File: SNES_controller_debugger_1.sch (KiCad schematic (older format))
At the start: 21 parts, among them J1 ICSP, J2 CONTROLLER_OUT, J3 MICRO_USB, SW1 Reset_switch, U1 ATmega32U4, Y1 16MHz

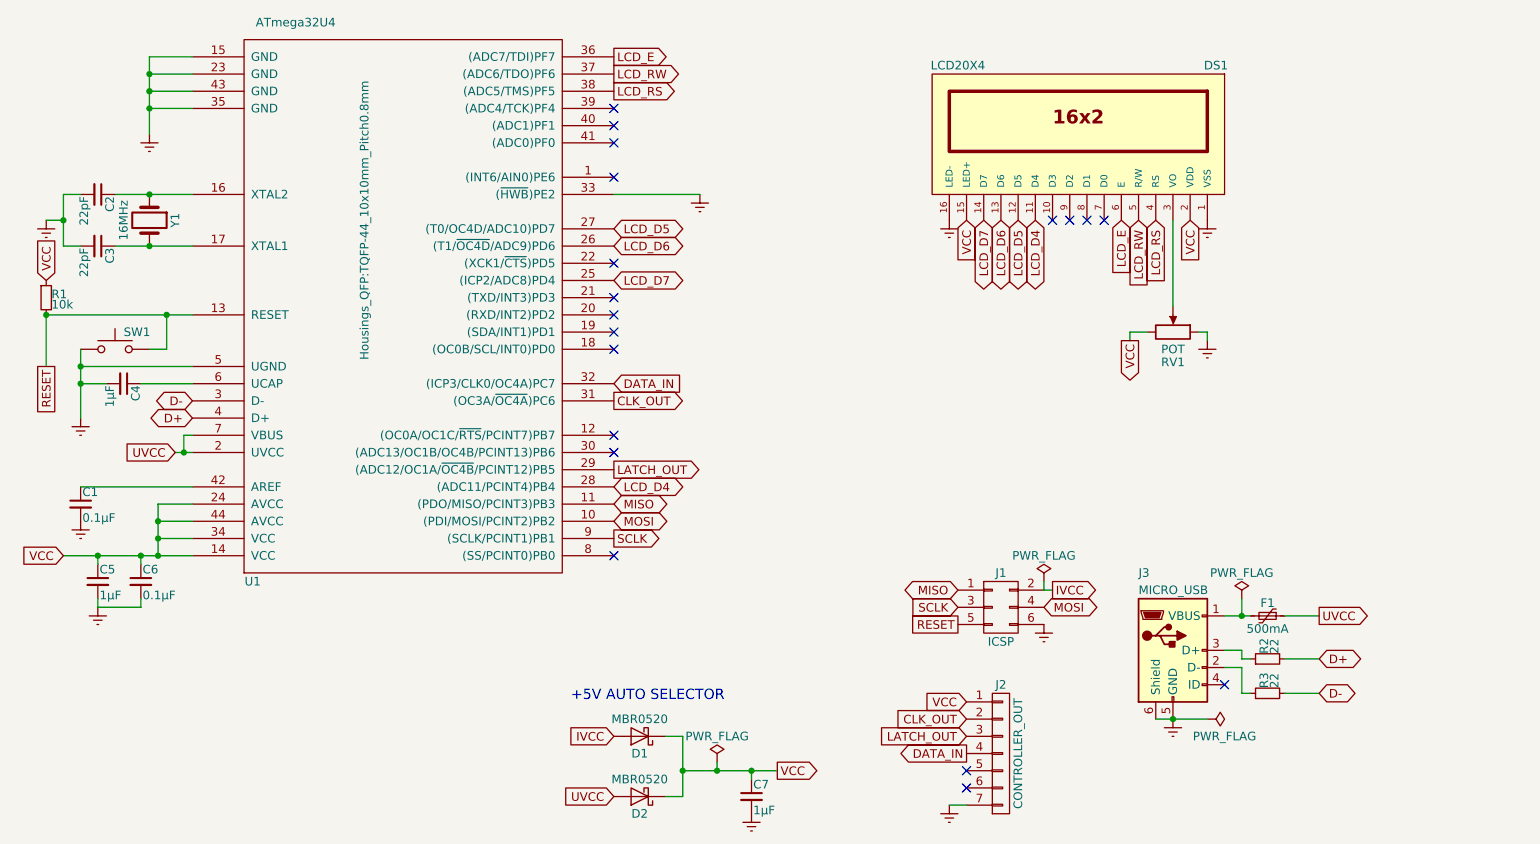
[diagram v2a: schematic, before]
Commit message: pcb: Add hardware capability to dim the LCD backlight and to switch power to the LCD
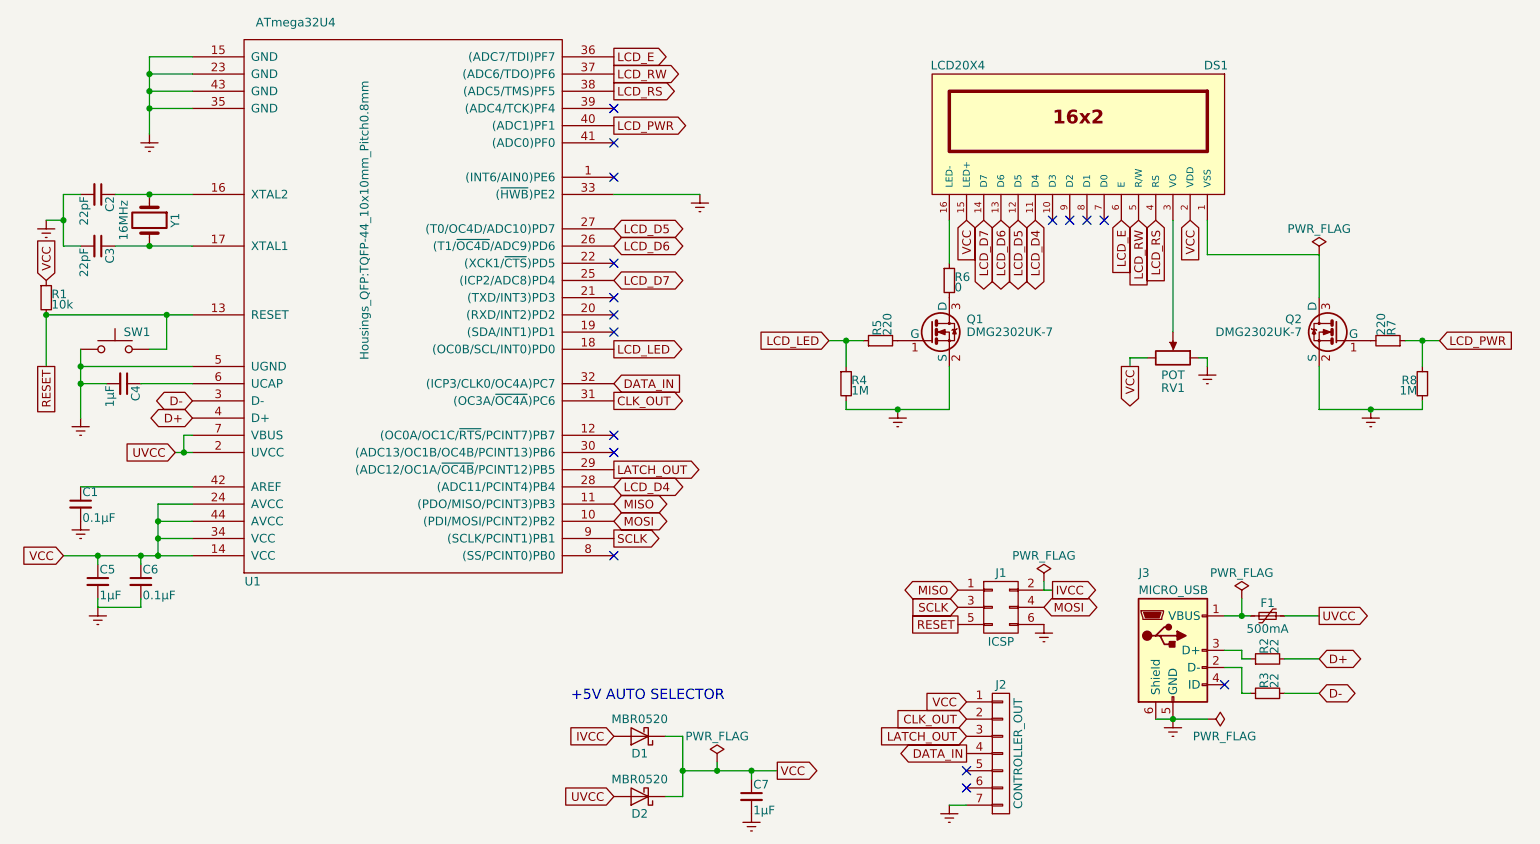
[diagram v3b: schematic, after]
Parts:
- added Q1, Q2: DMG2302UK-7, TO_SOT_Packages_SMD:SOT-23, symbol BSS138
- added R4, R8: 1M, Resistors_SMD:R_0603_HandSoldering, symbol R_Small
- added R5, R7: 220, Resistors_SMD:R_0603_HandSoldering, symbol R_Small
- added R6: 0, Resistors_SMD:R_0603_HandSoldering, symbol R_Small
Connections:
- net Earth: now also Q1.2 (S), Q2.2 (S), R4.2, R8.2; no longer DS1.1 (VSS), DS1.16 (LED-)
- net LCD_LED: now reaches U1.18 ((OC0B/SCL/INT0)PD0)
- net LCD_LED: now also R4.1, R5.1
- net LCD_PWR: now reaches U1.40 ((ADC1)PF1)
- net LCD_PWR: now also R7.1, R8.1
- new net: DS1.1 (VSS), Q2.3 (D)
- new net: DS1.16 (LED-), R6.1
- new net: Q1.3 (D), R6.2
- new net: Q1.1 (G), R5.2
- new net: Q2.1 (G), R7.2
- no-connect marks 19 -> 17
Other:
- moved on the sheet: RV1
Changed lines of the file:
@@
 L POT RV1
 U 1 1 591B92F6
-P 7200 3200
-F 0 "RV1" V 7025 3200 50  0000 C CNN
-F 1 "POT" V 7100 3200 50  0000 C CNN
-F 2 "Megaris_fixed_footprints:Potentiometer_Trimmer_Vishay_TS53YL" H 7200 3200 50  0001 C CNN
-F 3 "" H 7200 3200 50  0001 C CNN
-F 4 "TS53YL-10KCT-ND" V 7200 3200 60  0001 C CNN "Digi-Key part number"
-F 5 "TS53YL103MR10" V 7200 3200 60  0001 C CNN "MPN"
-	1    7200 3200
+P 7200 3350
+F 0 "RV1" V 7025 3350 50  0000 C CNN
+F 1 "POT" V 7100 3350 50  0000 C CNN
+F 2 "Megaris_fixed_footprints:Potentiometer_Trimmer_Vishay_TS53YL" H 7200 3350 50  0001 C CNN
+F 3 "" H 7200 3350 50  0001 C CNN
+F 4 "TS53YL-10KCT-ND" V 7200 3350 60  0001 C CNN "Digi-Key part number"
+F 5 "TS53YL103MR10" V 7200 3350 60  0001 C CNN "MPN"
+	1    7200 3350
 	0    1    -1   0
 $EndComp
@@
 $EndComp
 NoConn ~ 3950 1900
-NoConn ~ 3950 2000
 NoConn ~ 3950 2100
 NoConn ~ 3950 2300
-NoConn ~ 3950 2800
-NoConn ~ 3950 3300
 NoConn ~ 3950 3800
 NoConn ~ 3950 3900
@@
 $Comp
 L Earth #PWR01
-U 1 1 591D4C41
-P 7400 2550
-F 0 "#PWR01" H 7400 2300 50  0001 C CNN
-F 1 "Earth" H 7400 2400 50  0001 C CNN
-F 2 "" H 7400 2550 50  0001 C CNN
-F 3 "" H 7400 2550 50  0001 C CNN
-	1    7400 2550
-	1    0    0    -1
-$EndComp
-$Comp
-L Earth #PWR02
-U 1 1 591D4E59
-P 5900 2550
-F 0 "#PWR02" H 5900 2300 50  0001 C CNN
-F 1 "Earth" H 5900 2400 50  0001 C CNN
-F 2 "" H 5900 2550 50  0001 C CNN
-F 3 "" H 5900 2550 50  0001 C CNN
-	1    5900 2550
-	1    0    0    -1
-$EndComp
-$Comp
-L Earth #PWR03
 U 1 1 591D50E7
-P 7400 3250
-F 0 "#PWR03" H 7400 3000 50  0001 C CNN
-F 1 "Earth" H 7400 3100 50  0001 C CNN
-F 2 "" H 7400 3250 50  0001 C CNN
-F 3 "" H 7400 3250 50  0001 C CNN
-	1    7400 3250
+P 7400 3400
+F 0 "#PWR01" H 7400 3150 50  0001 C CNN
+F 1 "Earth" H 7400 3250 50  0001 C CNN
+F 2 "" H 7400 3400 50  0001 C CNN
+F 3 "" H 7400 3400 50  0001 C CNN
+	1    7400 3400
 	1    0    0    -1
 $EndComp
@@
 $EndComp
 $Comp
-L Earth #PWR04
+L Earth #PWR02
 U 1 1 591D5F38
 P 6450 4900
-F 0 "#PWR04" H 6450 4650 50  0001 C CNN
+F 0 "#PWR02" H 6450 4650 50  0001 C CNN
 F 1 "Earth" H 6450 4750 50  0001 C CNN
 F 2 "" H 6450 4900 50  0001 C CNN
@@
 $EndComp
 $Comp
-L Earth #PWR05
+L Earth #PWR03
 U 1 1 591D6035
 P 5900 5950
-F 0 "#PWR05" H 5900 5700 50  0001 C CNN
+F 0 "#PWR03" H 5900 5700 50  0001 C CNN
 F 1 "Earth" H 5900 5800 50  0001 C CNN
 F 2 "" H 5900 5950 50  0001 C CNN
@@
 $EndComp
 $Comp
-L Earth #PWR06
+L Earth #PWR04
 U 1 1 591D683F
 P 7200 5450
-F 0 "#PWR06" H 7200 5200 50  0001 C CNN
+F 0 "#PWR04" H 7200 5200 50  0001 C CNN
 F 1 "Earth" H 7200 5300 50  0001 C CNN
 F 2 "" H 7200 5450 50  0001 C CNN
@@
 NoConn ~ 3950 3100
 $Comp
-L PWR_FLAG #FLG07
+L PWR_FLAG #FLG05
 U 1 1 591D9550
 P 7400 5450
-F 0 "#FLG07" H 7400 5525 50  0001 C CNN
+F 0 "#FLG05" H 7400 5525 50  0001 C CNN
 F 1 "PWR_FLAG" V 7500 5550 50  0000 C CNN
 F 2 "" H 7400 5450 50  0001 C CNN
@@
 $EndComp
 $Comp
-L Earth #PWR08
+L Earth #PWR06
 U 1 1 591D9AF5
 P 650 2550
-F 0 "#PWR08" H 650 2300 50  0001 C CNN
+F 0 "#PWR06" H 650 2300 50  0001 C CNN
 F 1 "Earth" H 650 2400 50  0001 C CNN
 F 2 "" H 650 2550 50  0001 C CNN
@@
 $EndComp
 $Comp
-L Earth #PWR09
+L Earth #PWR07
 U 1 1 591D9C68
 P 850 3700
-F 0 "#PWR09" H 850 3450 50  0001 C CNN
+F 0 "#PWR07" H 850 3450 50  0001 C CNN
 F 1 "Earth" H 850 3550 50  0001 C CNN
 F 2 "" H 850 3700 50  0001 C CNN
@@
 $EndComp
 $Comp
-L Earth #PWR010
+L Earth #PWR08
 U 1 1 591D9CB5
 P 1250 2050
-F 0 "#PWR010" H 1250 1800 50  0001 C CNN
+F 0 "#PWR08" H 1250 1800 50  0001 C CNN
 F 1 "Earth" H 1250 1900 50  0001 C CNN
 F 2 "" H 1250 2050 50  0001 C CNN
@@
 $EndComp
 $Comp
-L Earth #PWR011
+L Earth #PWR09
 U 1 1 591D9D04
 P 850 4300
-F 0 "#PWR011" H 850 4050 50  0001 C CNN
+F 0 "#PWR09" H 850 4050 50  0001 C CNN
 F 1 "Earth" H 850 4150 50  0001 C CNN
 F 2 "" H 850 4300 50  0001 C CNN
@@
 $EndComp
 $Comp
-L PWR_FLAG #FLG012
+L PWR_FLAG #FLG010
 U 1 1 591DA503
 P 7600 4750
-F 0 "#FLG012" H 7600 4825 50  0001 C CNN
+F 0 "#FLG010" H 7600 4825 50  0001 C CNN
 F 1 "PWR_FLAG" H 7600 4900 50  0000 C CNN
 F 2 "" H 7600 4750 50  0001 C CNN
@@
 Text GLabel 3950 3500 2    50   Input ~ 0
 DATA_IN
-NoConn ~ 3950 3200
 $Comp
 L Polyfuse_Small F1
@@
 Text GLabel 7300 2550 3    50   Input ~ 0
 VCC
-Text GLabel 6000 2550 3    50   Input ~ 0
-VCC
-Text GLabel 6950 3250 3    50   Output ~ 0
+Text GLabel 6950 3400 3    50   Output ~ 0
 VCC
 Text GLabel 750  4500 0    50   Input ~ 0
@@
 IVCC
 $Comp
-L PWR_FLAG #FLG013
+L PWR_FLAG #FLG011
 U 1 1 591FC2B2
 P 6450 4650
-F 0 "#FLG013" H 6450 4725 50  0001 C CNN
+F 0 "#FLG011" H 6450 4725 50  0001 C CNN
 F 1 "PWR_FLAG" H 6450 4800 50  0000 C CNN
 F 2 "" H 6450 4650 50  0001 C CNN
@@
 VCC
 $Comp
-L PWR_FLAG #FLG014
+L PWR_FLAG #FLG012
 U 1 1 591FEDEE
 P 4550 5700
-F 0 "#FLG014" H 4550 5775 50  0001 C CNN
+F 0 "#FLG012" H 4550 5775 50  0001 C CNN
 F 1 "PWR_FLAG" H 4550 5850 50  0000 C CNN
 F 2 "" H 4550 5700 50  0001 C CNN
@@
 $EndComp
 $Comp
-L Earth #PWR015
+L Earth #PWR013
 U 1 1 59301178
 P 4450 2400
-F 0 "#PWR015" H 4450 2150 50  0001 C CNN
+F 0 "#PWR013" H 4450 2150 50  0001 C CNN
 F 1 "Earth" H 4450 2250 50  0001 C CNN
 F 2 "" H 4450 2400 50  0001 C CNN
@@
 $EndComp
 $Comp
-L Earth #PWR016
+L Earth #PWR014
 U 1 1 593021E9
 P 4750 6000
-F 0 "#PWR016" H 4750 5750 50  0001 C CNN
+F 0 "#PWR014" H 4750 5750 50  0001 C CNN
 F 1 "Earth" H 4750 5850 50  0001 C CNN
 F 2 "" H 4750 6000 50  0001 C CNN
@@
 $EndComp
 $Comp
-L Earth #PWR017
+L Earth #PWR015
 U 1 1 593033E6
 P 950 4800
-F 0 "#PWR017" H 950 4550 50  0001 C CNN
+F 0 "#PWR015" H 950 4550 50  0001 C CNN
 F 1 "Earth" H 950 4650 50  0001 C CNN
 F 2 "" H 950 4800 50  0001 C CNN
@@
 	1    0    0    -1
 $EndComp
+Text GLabel 3950 3300 2    50   Output ~ 0
+LCD_LED
 Wire Wire Line
 	6450 4650 6450 4700
@@
 	4350 5900 4250 5900
 Wire Wire Line
-	6950 3200 6950 3250
+	6950 3350 6950 3400
 Connection ~ 7200 5450
 Wire Wire Line
@@
 Connection ~ 1250 1700
 Wire Wire Line
-	7200 3050 7200 2550
-Wire Wire Line
-	7350 3200 7400 3200
-Wire Wire Line
-	7400 3200 7400 3250
-Wire Wire Line
-	7050 3200 6950 3200
+	7350 3350 7400 3350
+Wire Wire Line
+	7400 3350 7400 3400
+Wire Wire Line
+	7050 3350 6950 3350
 Wire Wire Line
 	1250 1600 1250 2050
@@
 	1500 4200 1300 4200
 Wire Wire Line
-	1300 4500 1300 4200
+	1300 4200 1300 4500
 Connection ~ 1300 4500
 Wire Wire Line
@@
 Wire Wire Line
 	7600 5100 7650 5100
+$Comp
+L R_Small R6
+U 1 1 598B7C95
+P 5900 2900
+F 0 "R6" H 5930 2920 50  0000 L CNN
+F 1 "0" H 5930 2860 50  0000 L CNN
+F 2 "Resistors_SMD:R_0603_HandSoldering" H 5900 2900 50  0001 C CNN
+F 3 "" H 5900 2900 50  0001 C CNN
+	1    5900 2900
+	1    0    0    -1
+$EndComp
+$Comp
+L Earth #PWR016
+U 1 1 598B7F8F
+P 5600 3650
+F 0 "#PWR016" H 5600 3400 50  0001 C CNN
+F 1 "Earth" H 5600 3500 50  0001 C CNN
+F 2 "" H 5600 3650 50  0001 C CNN
+F 3 "" H 5600 3650 50  0001 C CNN
+	1    5600 3650
+	1    0    0    -1
+$EndComp
+Text GLabel 6000 2550 3    50   Input ~ 0
+VCC
+Text GLabel 5200 3250 0    50   Input ~ 0
+LCD_LED
+$Comp
+L R_Small R5
+U 1 1 598B82E3
+P 5500 3250
+F 0 "R5" H 5530 3270 50  0000 L CNN
+F 1 "220" H 5530 3210 50  0000 L CNN
+F 2 "Resistors_SMD:R_0603_HandSoldering" H 5500 3250 50  0001 C CNN
+F 3 "" H 5500 3250 50  0001 C CNN
+	1    5500 3250
+	0    -1   -1   0
+$EndComp
+$Comp
+L BSS138 Q1
+U 1 1 598C915B
+P 5800 3200
+F 0 "Q1" H 6000 3275 50  0000 L CNN
+F 1 "DMG2302UK-7" H 6000 3200 50  0000 L CNN
+F 2 "TO_SOT_Packages_SMD:SOT-23" H 6000 3125 50  0001 L CIN
+F 3 "" H 5800 3200 50  0001 L CNN
+	1    5800 3200
+	1    0    0    -1
+$EndComp
+$Comp
+L R_Small R4
+U 1 1 598C9414
+P 5300 3500
+F 0 "R4" H 5330 3520 50  0000 L CNN
+F 1 "1M" H 5330 3460 50  0000 L CNN
+F 2 "Resistors_SMD:R_0603_HandSoldering" H 5300 3500 50  0001 C CNN
+F 3 "" H 5300 3500 50  0001 C CNN
+	1    5300 3500
+	1    0    0    -1
+$EndComp
+Wire Wire Line
+	5200 3250 5400 3250
+Wire Wire Line
+	5300 3250 5300 3400
+Connection ~ 5300 3250
+Wire Wire Line
+	5300 3650 5900 3650
+Wire Wire Line
+	5300 3600 5300 3650
+Connection ~ 5600 3650
+Text GLabel 3950 2000 2    50   Output ~ 0
+LCD_PWR
+$Comp
+L Earth #PWR017
+U 1 1 598CA9EA
+P 8350 3650
+F 0 "#PWR017" H 8350 3400 50  0001 C CNN
+F 1 "Earth" H 8350 3500 50  0001 C CNN
+F 2 "" H 8350 3650 50  0001 C CNN
+F 3 "" H 8350 3650 50  0001 C CNN
+	1    8350 3650
+	-1   0    0    -1
+$EndComp
+Text GLabel 8750 3250 2    50   Input ~ 0
+LCD_PWR
+$Comp
+L R_Small R7
+U 1 1 598CA9F1
+P 8450 3250
+F 0 "R7" H 8480 3270 50  0000 L CNN
+F 1 "220" H 8480 3210 50  0000 L CNN
+F 2 "Resistors_SMD:R_0603_HandSoldering" H 8450 3250 50  0001 C CNN
+F 3 "" H 8450 3250 50  0001 C CNN
+	1    8450 3250
+	0    1    -1   0
+$EndComp
+$Comp
+L BSS138 Q2
+U 1 1 598CA9F7
+P 8150 3200
+F 0 "Q2" H 8350 3275 50  0000 L CNN
+F 1 "DMG2302UK-7" H 8350 3200 50  0000 L CNN
+F 2 "TO_SOT_Packages_SMD:SOT-23" H 8350 3125 50  0001 L CIN
+F 3 "" H 8150 3200 50  0001 L CNN
+	1    8150 3200
+	-1   0    0    -1
+$EndComp
+$Comp
+L R_Small R8
+U 1 1 598CA9FD
+P 8650 3500
+F 0 "R8" H 8680 3520 50  0000 L CNN
+F 1 "1M" H 8680 3460 50  0000 L CNN
+F 2 "Resistors_SMD:R_0603_HandSoldering" H 8650 3500 50  0001 C CNN
+F 3 "" H 8650 3500 50  0001 C CNN
+	1    8650 3500
+	-1   0    0    -1
+$EndComp
+Wire Wire Line
+	8550 3250 8750 3250
+Wire Wire Line
+	8650 3250 8650 3400
+Connection ~ 8650 3250
+Wire Wire Line
+	8050 3650 8650 3650
+Wire Wire Line
+	8650 3650 8650 3600
+Connection ~ 8350 3650
+Wire Wire Line
+	7200 2550 7200 3200
+NoConn ~ 3950 3200
+Wire Wire Line
+	5900 3650 5900 3400
+Wire Wire Line
+	5900 2550 5900 2800
+Wire Wire Line
+	7400 2550 7400 2750
+Wire Wire Line
+	7400 2750 8050 2750
+Wire Wire Line
+	8050 2750 8050 3000
+Wire Wire Line
+	8050 3400 8050 3650
+$Comp
+L PWR_FLAG #FLG018
+U 1 1 598D1CF2
+P 8050 2750
+F 0 "#FLG018" H 8050 2825 50  0001 C CNN
+F 1 "PWR_FLAG" H 8050 2900 50  0000 C CNN
+F 2 "" H 8050 2750 50  0001 C CNN
+F 3 "" H 8050 2750 50  0001 C CNN
+	1    8050 2750
+	1    0    0    -1
+$EndComp
+NoConn ~ 3950 2800
 $EndSCHEMATC

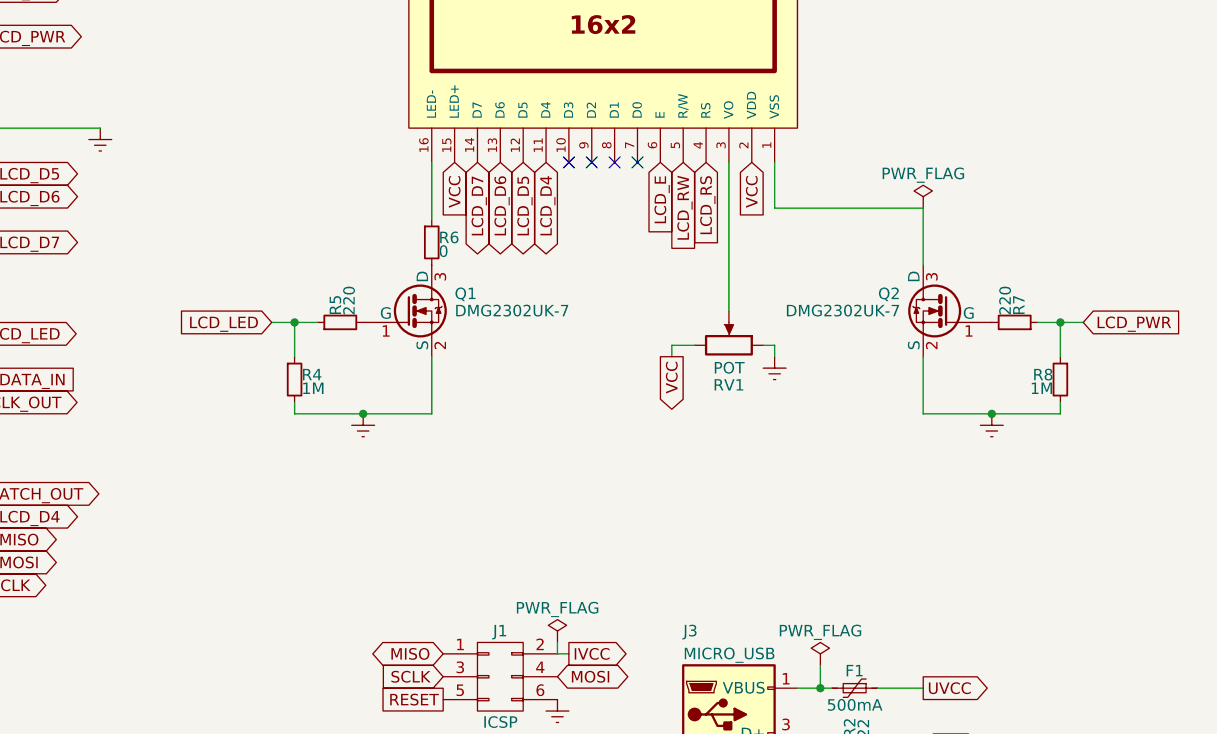
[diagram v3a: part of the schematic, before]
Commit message: pcb, firmware: Using an N-MOSFET to cut power to the LCD from the negative side won't work, so use a P-MOSFET on the positive side
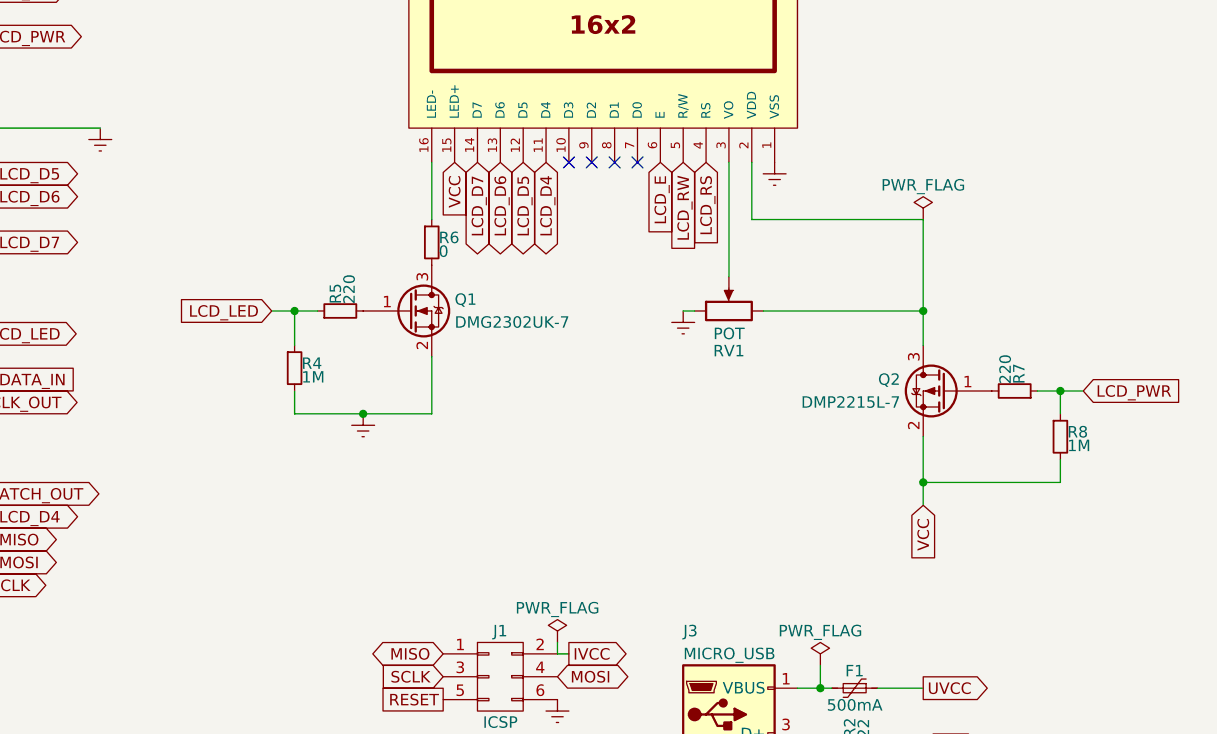
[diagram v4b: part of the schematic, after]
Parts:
- removed Q1, Q2: DMG2302UK-7, TO_SOT_Packages_SMD:SOT-23, symbol BSS138
- added Q1: DMG2302UK-7, TO_SOT_Packages_SMD:SOT-23_Handsoldering, symbol Q_NMOS_GSD
- added Q2: DMP2215L-7, TO_SOT_Packages_SMD:SOT-23_Handsoldering, symbol Q_PMOS_GSD
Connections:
- net Earth: now also DS1.1 (VSS), Q1.2 (S); no longer R8.2
- net VCC: now also R8.2, Q2.2 (S); no longer DS1.2 (VDD), RV1.3
- net at R6.2: now also Q1.3 (D)
- net at R5.2: now also Q1.1 (G)
- net at R7.2: now also Q2.1 (G)
- new net: DS1.2 (VDD), Q2.3 (D), RV1.3
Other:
- moved on the sheet: R4, R5, R7, RV1
